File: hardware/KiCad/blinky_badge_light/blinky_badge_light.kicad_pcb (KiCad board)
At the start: 4 copper layers, 108.6 x 87.7 mm, 120 parts, among them Q1 N-Channel MOSFET, Q2 Q_PMOS_GSD, Q3 N-Channel MOSFET, SW1 TS-1187A-B-A-B, U1 ESP32-S3-WROOM-1, U2 TP4056, U3 AP2112K-3.3, U4 MT3608, U5 CP2102N-Axx-xQFN24, U6 SN74LVC1T45DBV

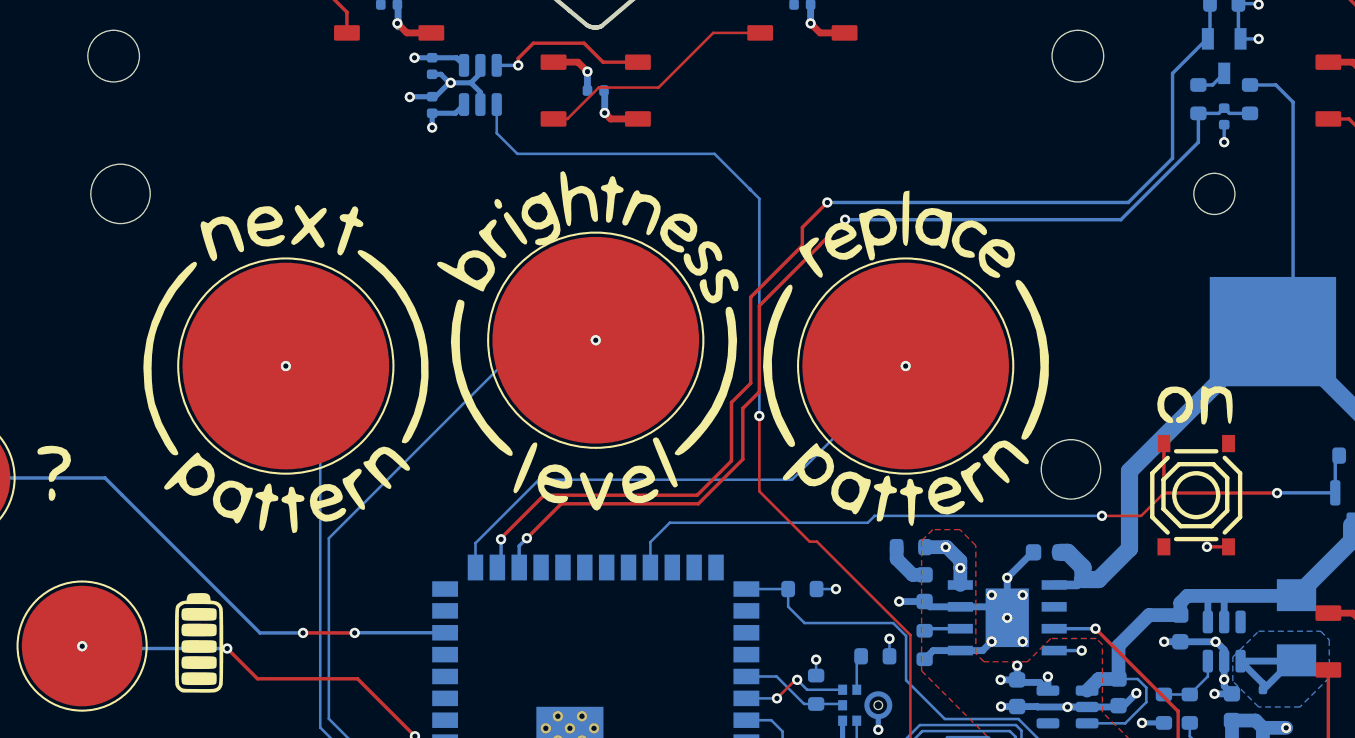
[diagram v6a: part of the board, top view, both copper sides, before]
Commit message: adding a bunch of qs and annotated items on schematic
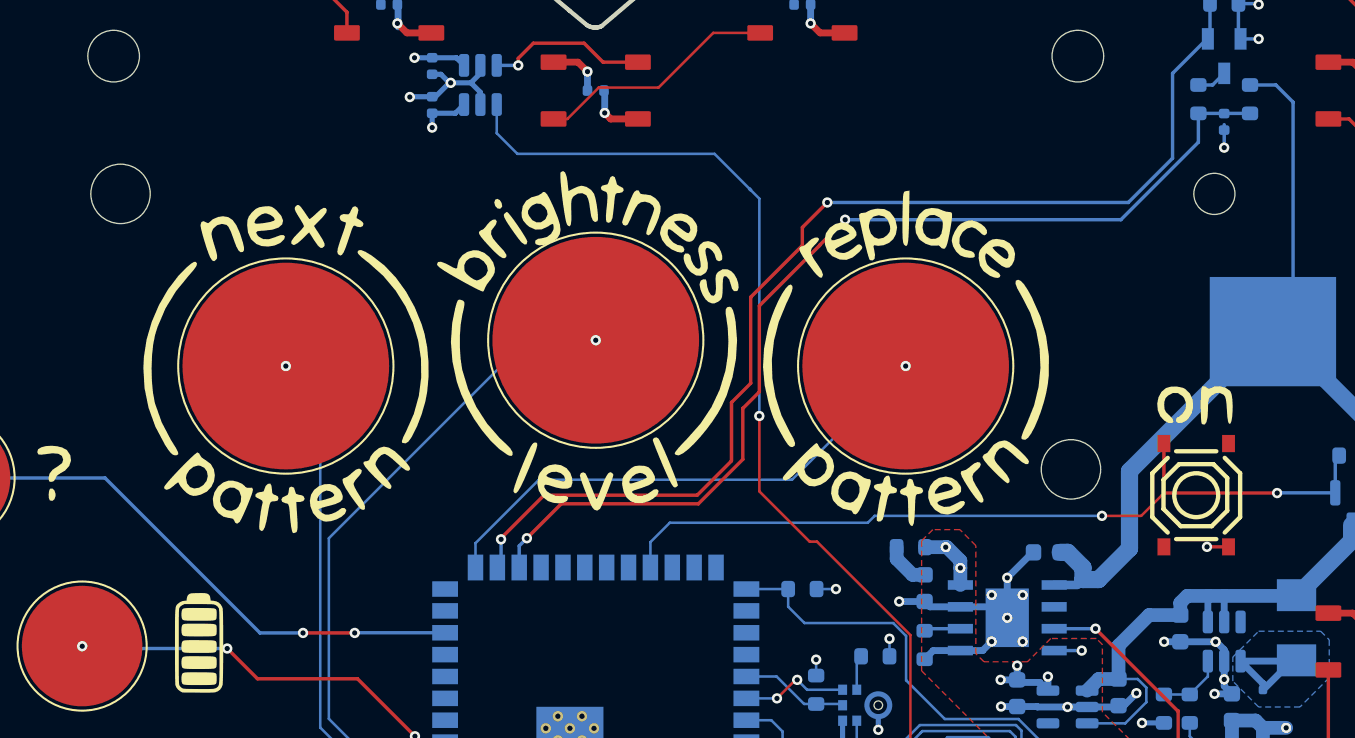
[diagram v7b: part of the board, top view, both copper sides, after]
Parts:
- added G***: LOGO, footprints:made_with_love, B.Cu at (125.2, 99.0)
- moved C41 0.32 mm to (186.5, 68.8)
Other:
- board text added: "Battery Monitoring Circuit"
- board text added: "Q1: is the thickness of the route from R13 to BAT+ ok or should it be thicker?"
- board text added: "Q2: should these two grounds be the same since they're adjacent?"
- board text added: "Q3: is it ok that the battery monitoring circuit is so far away from the ESP32?"
- board text added: "Q4: originally BAT- had a lot of thick connections to GND. Is what I have done here enough?"
- board text added: "Q5: this routing from battery monitoring to ESP32 is messy but not sure how to improve it.. had to do cross-over also.. open to suggestions"
- board text added: "Q6: when I do a crossover in routing is it better to make it longer or shorter (did both types here..)"
- board text added: "Q7a: is this pad too close to BAT -"
- board text added: "Q7b: is this pad too close to these assorted components?"
- board text added: "Q8: are the pads supposed to have exposed metal like the boards I got? (I'm just using the detault footprint..)"
- board text added: "Reverse Polarity Protection"

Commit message: review feedabck
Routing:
- net Net-(U1-GPIO6/TOUCH6/ADC1_CH5): track 38.6 -> 36.5 mm
- net Net-(U1-GPIO5/TOUCH5/ADC1_CH4): track 30.5 -> 29.2 mm
- net ESP32 Battery Monitoring Control: track 65.4 -> 64.6 mm
- net ESP32 Battery Monitoring: track 59.8 -> 60.3 mm
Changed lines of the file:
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@@
-	)
-	(segment
-		(start 146.7 89.6)
-		(end 143.015 93.285)
-		(width 0.15)
-		(layer "B.Cu")
-		(net 55)
 	)
 	(segment
@@
 	)
 	(segment
-		(start 161.4 89.6)
+		(start 146.05 90.25)
+		(end 160.75 90.25)
+		(width 0.15)
+		(layer "B.Cu")
+		(net 55)
+	)
+	(segment
+		(start 143.015 93.285)
+		(end 146.05 90.25)
+		(width 0.15)
+		(layer "B.Cu")
+		(net 55)
+	)
+	(segment
+		(start 160.75 90.25)
 		(end 168 83)
-		(width 0.15)
-		(layer "B.Cu")
-		(net 55)
-	)
-	(segment
-		(start 146.7 89.6)
-		(end 161.4 89.6)
 		(width 0.15)
 		(layer "B.Cu")
@@
 	)
 	(segment
-		(start 134 104)
-		(end 135.749 105.749)
-		(width 0.15)
-		(layer "B.Cu")
-		(net 57)
-	)
-	(segment
-		(start 136.845389 105.749)
-		(end 138.476388 107.38)
+		(start 139.52 107.38)
+		(end 134 101.86)
 		(width 0.15)
 		(layer "B.Cu")
@@
 	(segment
 		(start 134 85)
-		(end 134 104)
+		(end 134 101.86)
 		(width 0.15)
 		(layer "B.Cu")
@@
 	)
 	(segment
-		(start 135.749 105.749)
-		(end 136.845389 105.749)
+		(start 141.25 107.38)
+		(end 139.52 107.38)
 		(width 0.15)
 		(layer "B.Cu")
 		(net 57)
 	)
-	(segment
-		(start 138.476388 107.38)
-		(end 141.25 107.38)
-		(width 0.15)
-		(layer "B.Cu")
-		(net 57)
-	)
 	(via
 		(at 150 81.5)
@@
 		(drill 0.3)
 		(layers "F.Cu" "B.Cu")
-		(net 58)
-	)
-	(segment
-		(start 136.409223 105.398)
-		(end 136.699999 105.397999)
-		(width 0.15)
-		(layer "B.Cu")
-		(net 58)
-	)
-	(segment
-		(start 146 81.5)
-		(end 134.5 93)
-		(width 0.15)
-		(layer "B.Cu")
-		(net 58)
-	)
-	(segment
-		(start 136.699999 105.397999)
-		(end 136.699998 105.398)
-		(width 0.15)
-		(layer "B.Cu")
-		(net 58)
-	)
-	(segment
-		(start 136.699998 105.398)
-		(end 136.990777 105.398)
-		(width 0.15)
-		(layer "B.Cu")
-		(net 58)
-	)
-	(segment
-		(start 136.990777 105.398)
-		(end 137.702776 106.11)
-		(width 0.15)
-		(layer "B.Cu")
 		(net 58)
 	)
@@
 	)
 	(segment
-		(start 134.5 93)
-		(end 134.5 103.488777)
+		(start 135.19 92.31)
+		(end 135.19 101.56)
 		(width 0.15)
 		(layer "B.Cu")
@@
 	)
 	(segment
-		(start 134.5 103.488777)
-		(end 136.409223 105.398)
+		(start 135.19 101.56)
+		(end 139.74 106.11)
 		(width 0.15)
 		(layer "B.Cu")
@@
 	)
 	(segment
-		(start 137.702776 106.11)
+		(start 146 81.5)
+		(end 135.19 92.31)
+		(width 0.15)
+		(layer "B.Cu")
+		(net 58)
+	)
+	(segment
+		(start 139.74 106.11)
 		(end 141.25 106.11)
 		(width 0.15)
@@
 	)
 	(segment
-		(start 146 93)
-		(end 148 91)
-		(width 0.2)
-		(layer "F.Cu")
-		(net 83)
-	)
-	(segment
-		(start 155.958999 91)
-		(end 158.540799 88.4182)
-		(width 0.2)
-		(layer "F.Cu")
-		(net 83)
-	)
-	(segment
-		(start 164.485901 74.5)
-		(end 163 75.985901)
-		(width 0.2)
-		(layer "F.Cu")
-		(net 83)
-	)
-	(segment
-		(start 159.5 79.5)
-		(end 159.5 84.5)
-		(width 0.2)
-		(layer "F.Cu")
-		(net 83)
-	)
-	(segment
-		(start 163 76)
-		(end 159.5 79.5)
-		(width 0.2)
-		(layer "F.Cu")
-		(net 83)
-	)
-	(segment
-		(start 158.540799 88.4182)
-		(end 158.540799 85.459201)
+		(start 148 91)
+		(end 146 93)
+		(width 0.2)
+		(layer "F.Cu")
+		(net 83)
+	)
+	(segment
+		(start 163.6 74.5)
+		(end 159.5 78.6)
 		(width 0.2)
 		(layer "F.Cu")
@@
 	)
 	(segment
-		(start 163 75.985901)
-		(end 163 76)
-		(width 0.2)
-		(layer "F.Cu")
-		(net 83)
-	)
-	(segment
-		(start 148 91)
+		(start 158.540799 85.459201)
+		(end 158.540799 88.4182)
+		(width 0.2)
+		(layer "F.Cu")
+		(net 83)
+	)
+	(segment
+		(start 158.540799 88.4182)
 		(end 155.958999 91)
 		(width 0.2)
@@
 		(net 83)
 	)
+	(segment
+		(start 159.5 78.6)
+		(end 159.5 84.5)
+		(width 0.2)
+		(layer "F.Cu")
+		(net 83)
+	)
+	(segment
+		(start 155.958999 91)
+		(end 148 91)
+		(width 0.2)
+		(layer "F.Cu")
+		(net 83)
+	)
+	(segment
+		(start 164.485901 74.5)
+		(end 163.6 74.5)
+		(width 0.2)
+		(layer "F.Cu")
+		(net 83)
+	)
 	(via
 		(at 164.485901 74.5)
@@
 		(drill 0.3)
 		(layers "F.Cu" "B.Cu")
+		(net 83)
+	)
+	(segment
+		(start 181.59 73.41)
+		(end 185 70)
+		(width 0.2)
+		(layer "B.Cu")
+		(net 83)
+	)
+	(segment
+		(start 165.575901 73.41)
+		(end 181.59 73.41)
+		(width 0.2)
+		(layer "B.Cu")
 		(net 83)
 	)
@@
 	)
 	(segment
+		(start 164.485901 74.5)
+		(end 165.575901 73.41)
+		(width 0.2)
+		(layer "B.Cu")
+		(net 83)
+	)
+	(segment
 		(start 186.508212 68.325)
 		(end 186.497839 68.335373)
@@
 	)
 	(segment
-		(start 164.485901 74.5)
-		(end 180.5 74.5)
-		(width 0.2)
-		(layer "B.Cu")
-		(net 83)
-	)
-	(segment
 		(start 145.555 93.445)
 		(end 145.555 94.7)
@@
 	)
 	(segment
-		(start 180.5 74.5)
-		(end 185 70)
-		(width 0.2)
-		(layer "B.Cu")
-		(net 83)
+		(start 159 77.949468)
+		(end 159 84)
+		(width 0.2)
+		(layer "F.Cu")
+		(net 102)
+	)
+	(segment
+		(start 157.883127 88.508772)
+		(end 155.891899 90.5)
+		(width 0.2)
+		(layer "F.Cu")
+		(net 102)
+	)
+	(segment
+		(start 159 84)
+		(end 157.883127 85.116873)
+		(width 0.2)
+		(layer "F.Cu")
+		(net 102)
+	)
+	(segment
+		(start 144.5 93)
+		(end 144.5 93.062915)
+		(width 0.2)
+		(layer "F.Cu")
+		(net 102)
+	)
+	(segment
+		(start 147 90.5)
+		(end 144.5 93)
+		(width 0.2)
+		(layer "F.Cu")
+		(net 102)
 	)
 	(segment
@@
 	)
 	(segment
-		(start 162 74.949468)
-		(end 162 76)
+		(start 163.449468 73.5)
+		(end 159 77.949468)
 		(width 0.2)
 		(layer "F.Cu")
@@
 		(net 102)
 	)
-	(segment
-		(start 163.449468 73.5)
-		(end 162 74.949468)
-		(width 0.2)
-		(layer "F.Cu")
-		(net 102)
-	)
-	(segment
-		(start 144.5 93)
-		(end 144.5 93.062915)
-		(width 0.2)
-		(layer "F.Cu")
-		(net 102)
-	)
-	(segment
-		(start 147 90.5)
-		(end 144.5 93)
-		(width 0.2)
-		(layer "F.Cu")
-		(net 102)
-	)
-	(segment
-		(start 157.883127 88.508772)
-		(end 155.891899 90.5)
-		(width 0.2)
-		(layer "F.Cu")
-		(net 102)
-	)
-	(segment
-		(start 159 79)
-		(end 159 84)
-		(width 0.2)
-		(layer "F.Cu")
-		(net 102)
-	)
-	(segment
-		(start 162 76)
-		(end 159 79)
-		(width 0.2)
-		(layer "F.Cu")
-		(net 102)
-	)
-	(segment
-		(start 159 84)
-		(end 157.883127 85.116873)
-		(width 0.2)
-		(layer "F.Cu")
-		(net 102)
-	)
 	(via
 		(at 163.449468 73.5)
@@
 		(drill 0.3)
 		(layers "F.Cu" "B.Cu")
-		(net 102)
-	)
-	(segment
-		(start 185.55 64)
-		(end 185.5 64)
-		(width 0.2)
-		(layer "B.Cu")
 		(net 102)
 	)
@@
 	)
 	(segment
-		(start 180.9329 73.5)
-		(end 183.5 70.9329)
-		(width 0.2)
-		(layer "B.Cu")
-		(net 102)
-	)
-	(segment
-		(start 163.449468 73.5)
-		(end 180.9329 73.5)
-		(width 0.2)
-		(layer "B.Cu")
-		(net 102)
-	)
-	(segment
 		(start 185.5 64)
-		(end 183.5 66)
+		(end 185.55 64)
 		(width 0.2)
 		(layer "B.Cu")
@@
 	(segment
 		(start 183.5 66)
-		(end 183.5 70.9329)
+		(end 185.5 64)
+		(width 0.2)
+		(layer "B.Cu")
+		(net 102)
+	)
+	(segment
+		(start 180.49 72.69)
+		(end 183.5 69.68)
+		(width 0.2)
+		(layer "B.Cu")
+		(net 102)
+	)
+	(segment
+		(start 163.449468 73.5)
+		(end 164.259468 72.69)
 		(width 0.2)
 		(layer "B.Cu")
@@
 		(width 0.2)
 		(layer "B.Cu")
+		(net 102)
+	)
+	(segment
+		(start 183.5 69.68)
+		(end 183.5 66)
+		(width 0.2)
+		(layer "B.Cu")
+		(net 102)
+	)
+	(segment
+		(start 164.259468 72.69)
+		(end 180.49 72.69)
+		(width 0.2)
+		(layer "B.Cu")
